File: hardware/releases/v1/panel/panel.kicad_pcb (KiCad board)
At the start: 4 copper layers, 140.5 x 63.1 mm, 219 parts, among them J1 12-32V + RS485, J101 Main board, J102 XD_N, J103 XD_E, J104 XD_S, J105 XD_W, J106 PIEZO_NE, J107 PIEZO_NW, J108 PIEZO_SW, J109 PIEZO_SE, J110 DOME_SOCKET, J111 AUX 12V_HEAT, J112 SWD, J2 Crown board, J201 Probe T-Header SMD, J3 Probe board, J301 CROWN_RISER, J4 PMSA003I PM, J401 Main board, J402 Reflector T-Socket SMD, J5 Power board, J501 Main board, Q1 AO3400A, Q401 AO3400A, SW1 SERVICE, U101 STM32G431RBT6, U102 UCC27524ADR, U103 UCC27524ADR, U104 UCC27524ADR, U105 UCC27524ADR, U106 MMC5603NJ, U107 74HC4052D, U108 TLV9062IDR, U109 AS3935-BQFT, U110 XC6206P332MR, U2 LM66100, U3 XIAO ESP32C6, U301 LTR-390UV-01, U302 TSL25911FN, U303 GUVB-C31SM, U4 ADS1115IDGSR, U401 SCD41-D-R2, U402 SGP41-D-R4, U403 SHT40-AD1F-R2, U404 LM2903DR2G, U405 BMP585, U5 LSM6DS3TR-C, U501 TPS54360DDAR, U502 TPS54360DDAR, U503 AP2112K-3.3, U7 SP3485EN-L/TR, Y101 8MHz

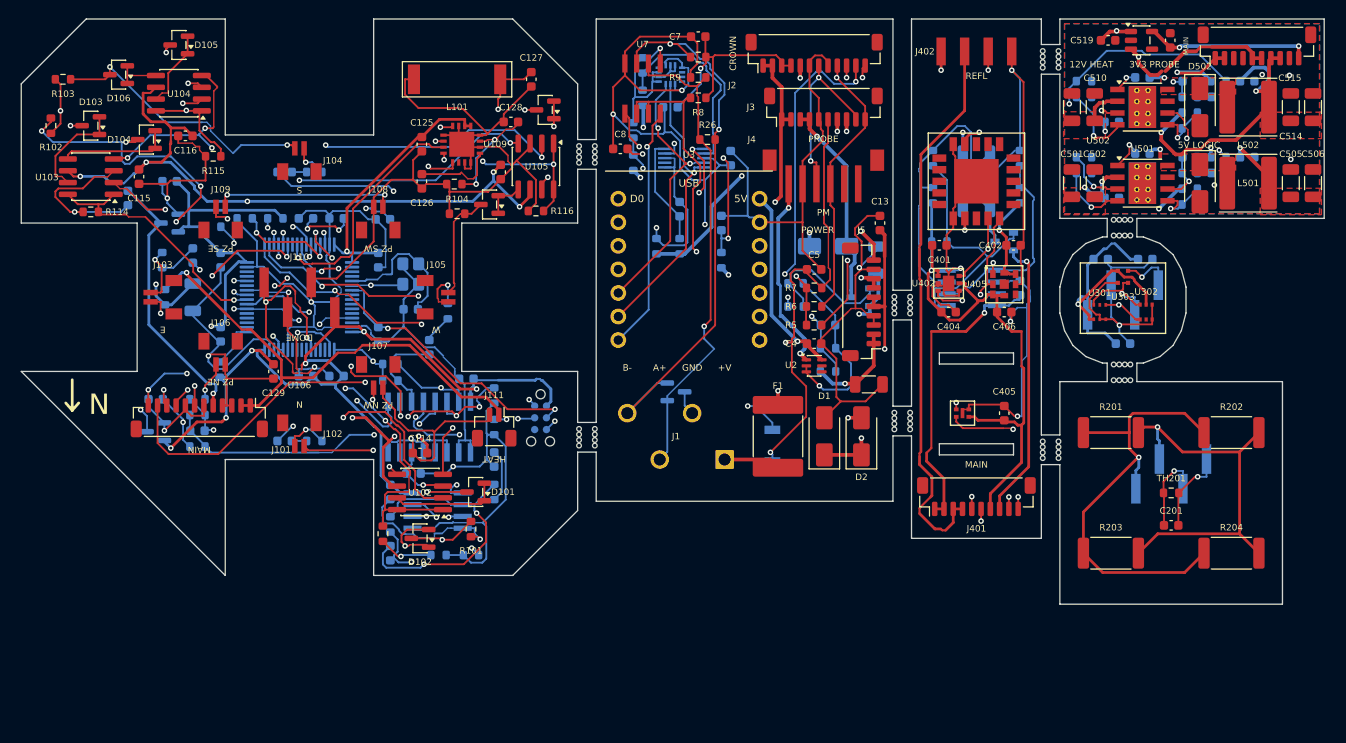
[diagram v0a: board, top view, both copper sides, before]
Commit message: Update dome PCB to Genicom GUVB-C21SD/GUVA-C22SD photodiodes with TLV9062 transimpedance and ADS1115 ADC, increase diameter to Ø 15.6 mm
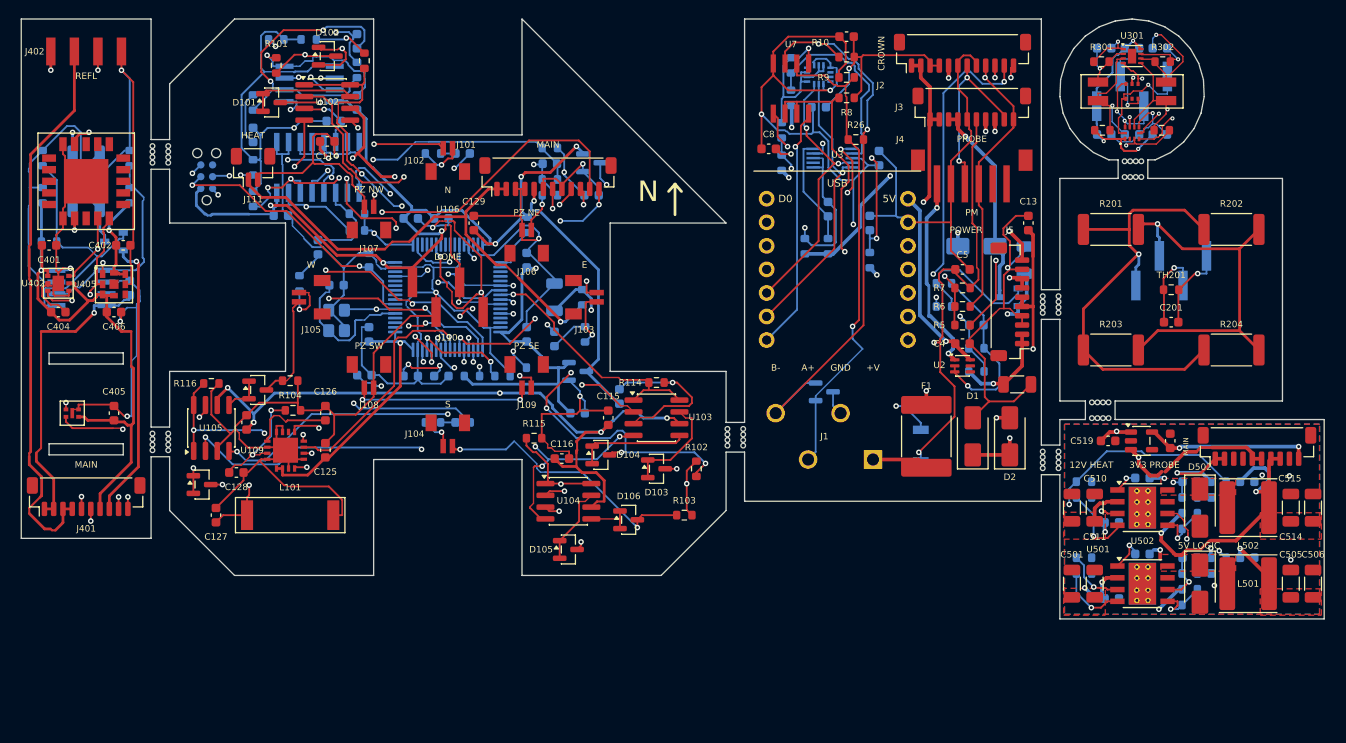
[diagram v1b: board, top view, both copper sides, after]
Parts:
- added C304: 10n 50V, Capacitor_SMD:C_0603_1608Metric, B.Cu at (116.8, 3.15)
- added C305: 22n 50V, Capacitor_SMD:C_0603_1608Metric, B.Cu at (122.8, 3.15)
- added C306: 1u 50V, Capacitor_SMD:C_0603_1608Metric, B.Cu at (119.8, 12.4)
- added D301: GUVB-C21SD, gateway_fp:Genicom_COB2418, F.Cu at (116.1, 7.80)
- added D302: GUVA-C22SD, gateway_fp:Genicom_COB2418, F.Cu at (123.5, 7.80)
- added R301: 10M, Resistor_SMD:R_0603_1608Metric, F.Cu at (116.5, 4.60)
- added R302: 4M7, Resistor_SMD:R_0603_1608Metric, F.Cu at (123.1, 4.60)
- added R303: 100k, Resistor_SMD:R_0603_1608Metric, F.Cu at (116.6, 12.0)
- added R304: 10k, Resistor_SMD:R_0603_1608Metric, F.Cu at (123.0, 12.0)
- C303: value 1u 50V -> 100n 50V
- U301: value LTR-390UV-01 -> TLV9062IDSGR; footprint gateway_fp:LiteOn_LTR-390UV-01 -> Package_SON:Texas_DSG0008A_WSON-8-1EP_2x2mm_P0.5mm_EP0.9x1.6mm
- U303: value GUVB-C31SM -> ADS1115IRUGR; footprint gateway_fp:GenUV_GUVB-C31SM -> gateway_fp:TI_ADS1115_X2QFN-10
- moved C401 96.0 mm to (3.00, 24.4)
- moved C402 96.0 mm to (11.0, 24.4)
- moved C403 96.0 mm to (11.7, 29.0)
- moved C404 96.0 mm to (4.00, 31.6)
- moved C405 96.0 mm to (10.0, 42.5)
- moved C406 96.0 mm to (10.0, 31.6)
- moved J401 96.0 mm to (7.00, 51.5)
- moved J402 96.0 mm to (7.00, 3.50)
- moved Q401 96.0 mm to (10.0, 24.0)
- moved R401 96.0 mm to (7.00, 20.5)
- moved R402 96.0 mm to (7.00, 14.5)
- moved R403 96.0 mm to (2.30, 19.0)
- moved R404 96.0 mm to (11.7, 19.0)
- moved R405 96.0 mm to (11.7, 15.0)
- moved R406 96.0 mm to (3.00, 24.0)
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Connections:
- U301 pad 1: DOME_+3V3 -> DOME_UVB_OUT
- U301 pad 2: DOME_GND -> DOME_UVB_IN
- U301 pad 3: DOME_GND -> DOME_UV_VB
- U301 pad 4: DOME_I2C_SCL -> DOME_GND
- U301 pad 5: (no net) -> DOME_UV_VB
- U301 pad 6: DOME_I2C_SDA -> DOME_UVA_IN
- U303 pad 1: DOME_GND -> DOME_+3V3
- U303 pad 2: DOME_I2C_SDA -> (no net)
- U303 pad 3: DOME_I2C_SCL -> DOME_GND
- U303 pad 4: DOME_+3V3 -> DOME_UVB_OUT
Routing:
- net DOME_UV_VB: track 0.00 -> 34.9 mm, vias 0 -> 2
- net DOME_UVB_OUT: track 0.00 -> 26.0 mm, vias 0 -> 2
- net DOME_UVA_OUT: track 0.00 -> 17.1 mm, vias 0 -> 2
- net DOME_UVA_IN: track 0.00 -> 12.8 mm, vias 0 -> 1
- net DOME_UVB_IN: track 0.00 -> 7.04 mm, vias 0 -> 1
- net DOME_I2C_SDA: track 11.7 -> 9.79 mm, vias 1 -> 2
- net DOME_I2C_SCL: track 14.2 -> 12.8 mm, vias 2 -> 1
- net DOME_+3V3: track 33.3 -> 32.9 mm, vias 1 -> 5
- net DOME_GND: track 29.0 -> 29.1 mm, vias 1 -> 4
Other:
- board size 140.5 x 63.1 mm -> 140.5 x 64.7 mm

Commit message: Update dome PCB layout with manual reference and label placement, add Stock_Optional field for LTR-390UV-01 sensor to allow JLC assembly when in stock without failing release on shortage
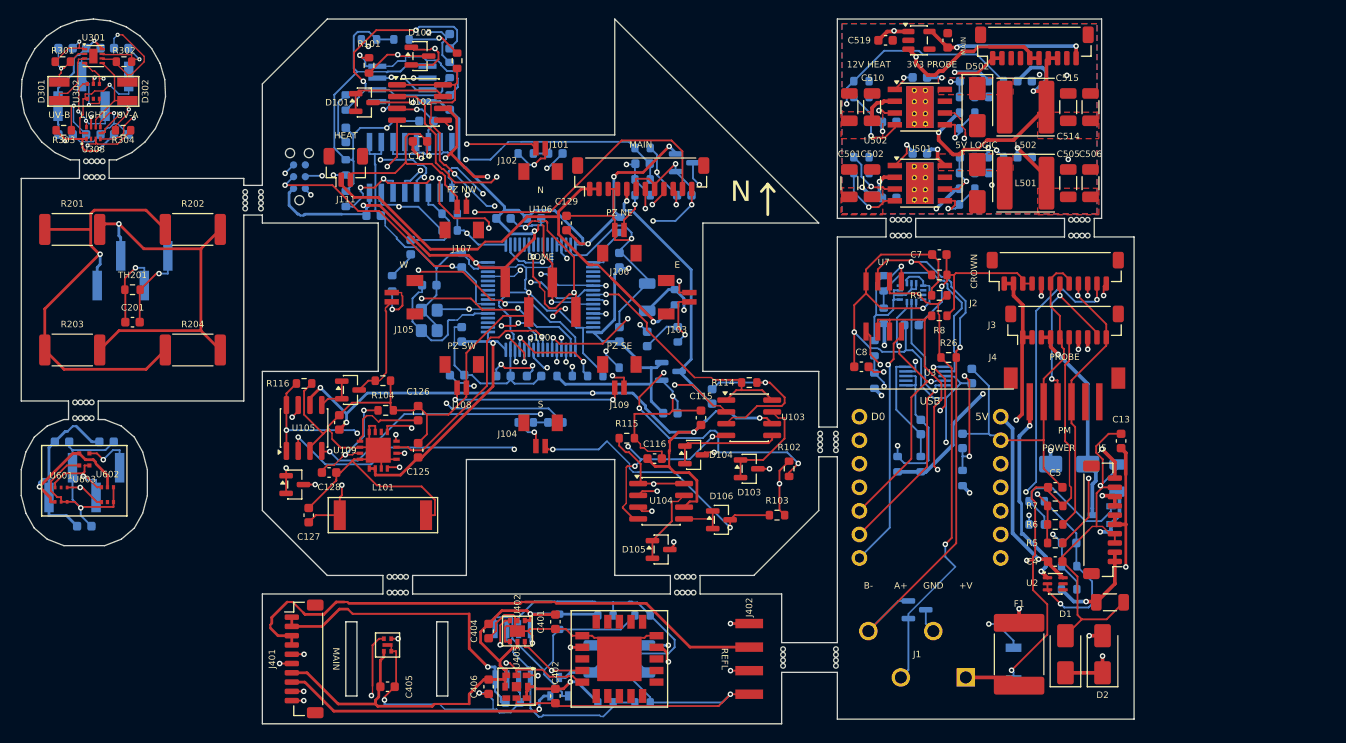
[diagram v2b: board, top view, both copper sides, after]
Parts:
- added C601: 100n 50V, Capacitor_SMD:C_0603_1608Metric, B.Cu at (4.40, 45.6)
- added C602: 100n 50V, Capacitor_SMD:C_0603_1608Metric, B.Cu at (9.20, 45.6)
- added C603: 1u 50V, Capacitor_SMD:C_0603_1608Metric, B.Cu at (6.80, 54.7)
- added J601: CROWN_RISER, gateway_fp:HX_PZ2.54-1x4P-SMD, B.Cu at (6.80, 50.0)
- added U601: LTR-390UV-01, gateway_fp:LiteOn_LTR-390UV-01, F.Cu at (4.30, 51.3)
- added U602: TSL25911FN, gateway_fp:AMS_TSL25911FN, F.Cu at (9.30, 51.3)
- added U603: GUVB-C31SM, gateway_fp:GenUV_GUVB-C31SM, F.Cu at (6.80, 47.5)
- moved C201 112.0 mm to (12.0, 32.7)
- moved C301 112.0 mm to (10.8, 12.4)
- moved C302 112.0 mm to (7.78, 3.15)
- moved C303 112.0 mm to (4.78, 12.4)
- moved C304 112.0 mm to (4.78, 3.15)
- moved C305 112.0 mm to (10.8, 3.15)
- moved C306 112.0 mm to (7.78, 12.4)
- moved D301 112.0 mm to (4.11, 7.80)
- moved D302 112.0 mm to (11.4, 7.80)
- moved J201 112.0 mm to (12.0, 27.1)
- moved J301 112.0 mm to (7.78, 7.80)
- moved R201 112.0 mm to (5.50, 22.7)
- moved R202 112.0 mm to (18.5, 22.7)
- moved R203 112.0 mm to (5.50, 35.7)
- moved R204 112.0 mm to (18.5, 35.7)
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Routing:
- net DOME_LEGACY_+3V3: track 0.00 -> 33.3 mm, vias 0 -> 1
- net DOME_LEGACY_GND: track 0.00 -> 29.5 mm, vias 0 -> 1
- net DOME_LEGACY_I2C_SCL: track 0.00 -> 14.2 mm, vias 0 -> 2
- net DOME_LEGACY_I2C_SDA: track 0.00 -> 11.7 mm, vias 0 -> 1
- net CROWN_GND: track 325.9 -> 335.4 mm
- net PROBE_GND: track 95.7 -> 98.7 mm
- net GND: track 169.1 -> 170.9 mm
- net POWER_LOGIC_SW: track 1.65 -> 3.39 mm
- net POWER_+5V: track 59.6 -> 60.8 mm
- net DOME_GND: track 29.1 -> 30.1 mm
- net POWER_VIN_PROT: track 47.0 -> 47.9 mm
- added copper zone on In1.Cu, net DOME_LEGACY_GND
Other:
- board size 140.5 x 64.7 mm -> 120 x 76 mm
- board text added: "LIGHT"
- board text added: "UV-A"
- board text added: "UV-B"

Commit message: Update AS3935 lightning antenna to dual land pattern supporting Coilcraft MA5532-AE or Premo SDTR1103-HF1-0100J with adjusted Q damping resistor notes, and reorganize self-assembly order files to LCSC-only and elsewhere CSVs with multi-distributor columns
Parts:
- L101: footprint RF_Antenna:Coilcraft_MA5532-AE_RFID -> gateway_fp:AS3935_Antenna_MA5532_SDTR1103
